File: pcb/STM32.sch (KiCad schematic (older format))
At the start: 31 parts, among them J1 Conn_02x07_Odd_Even, X1 ABM8G

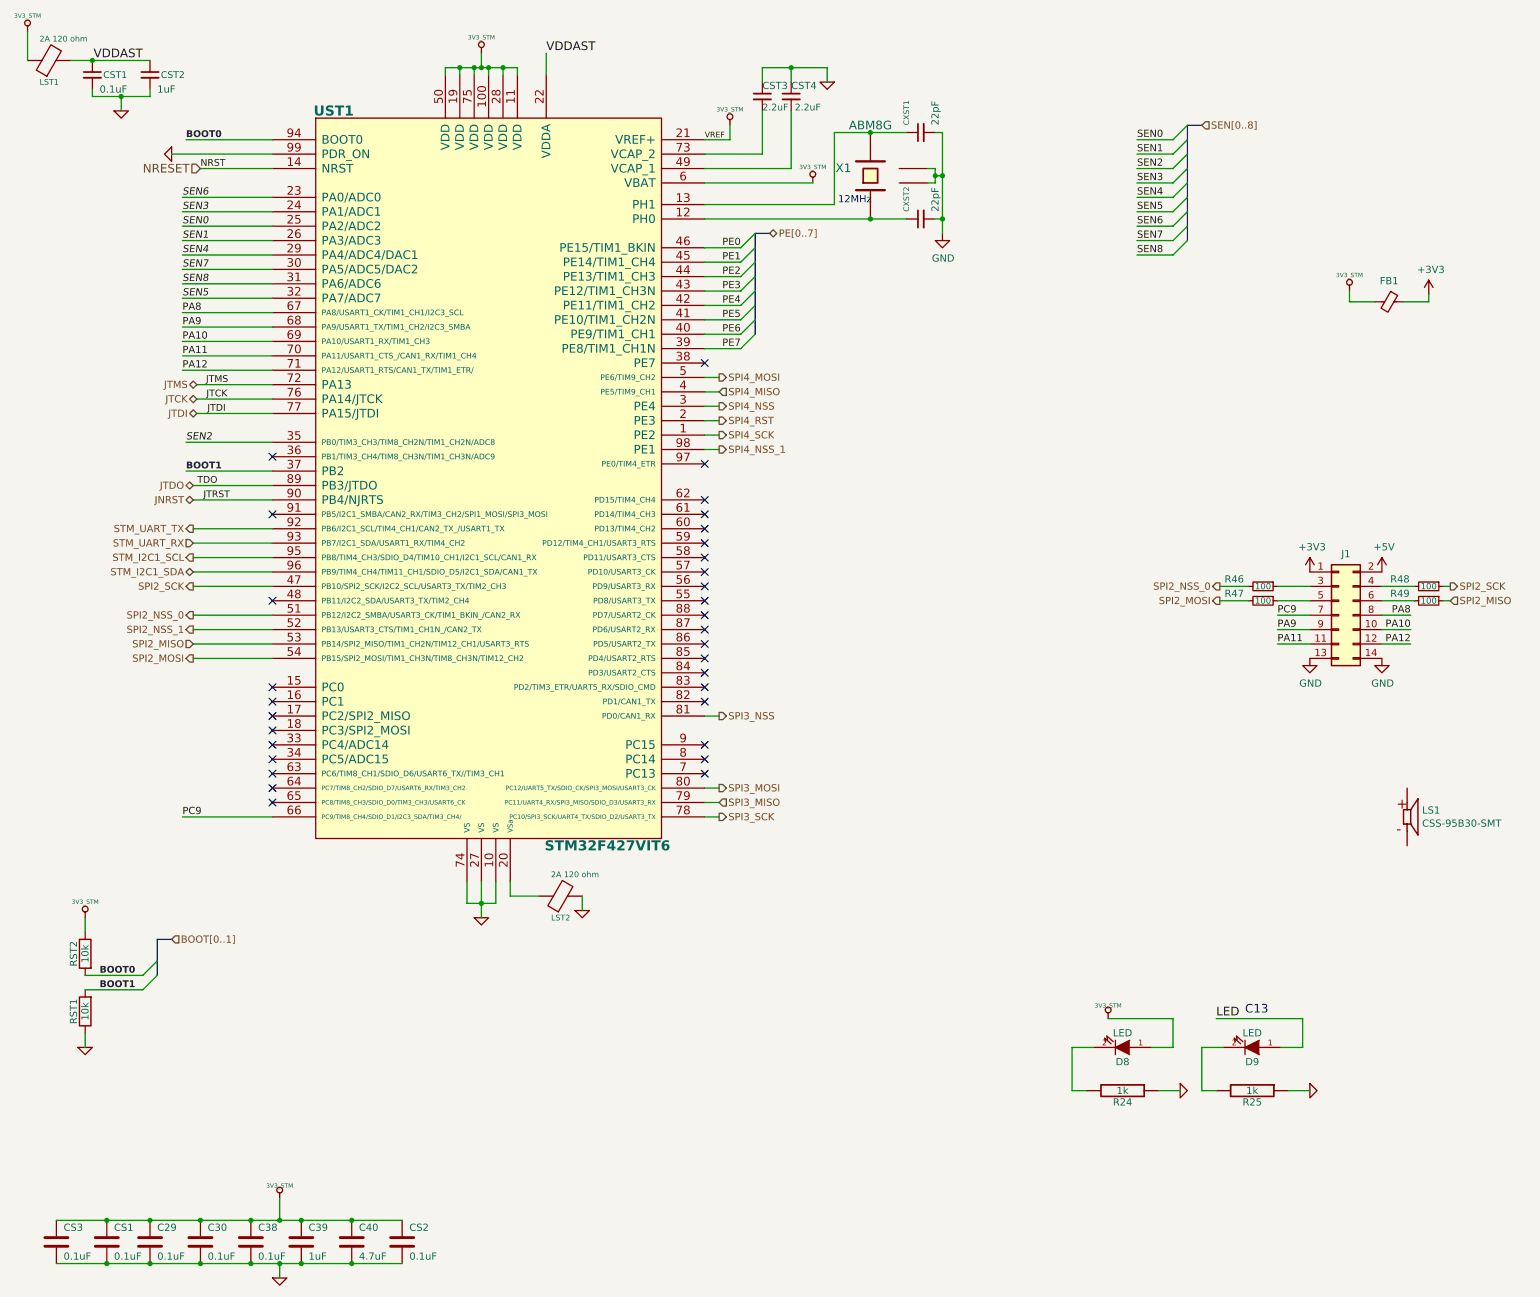
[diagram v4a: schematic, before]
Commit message: Buzzer circuit on schema
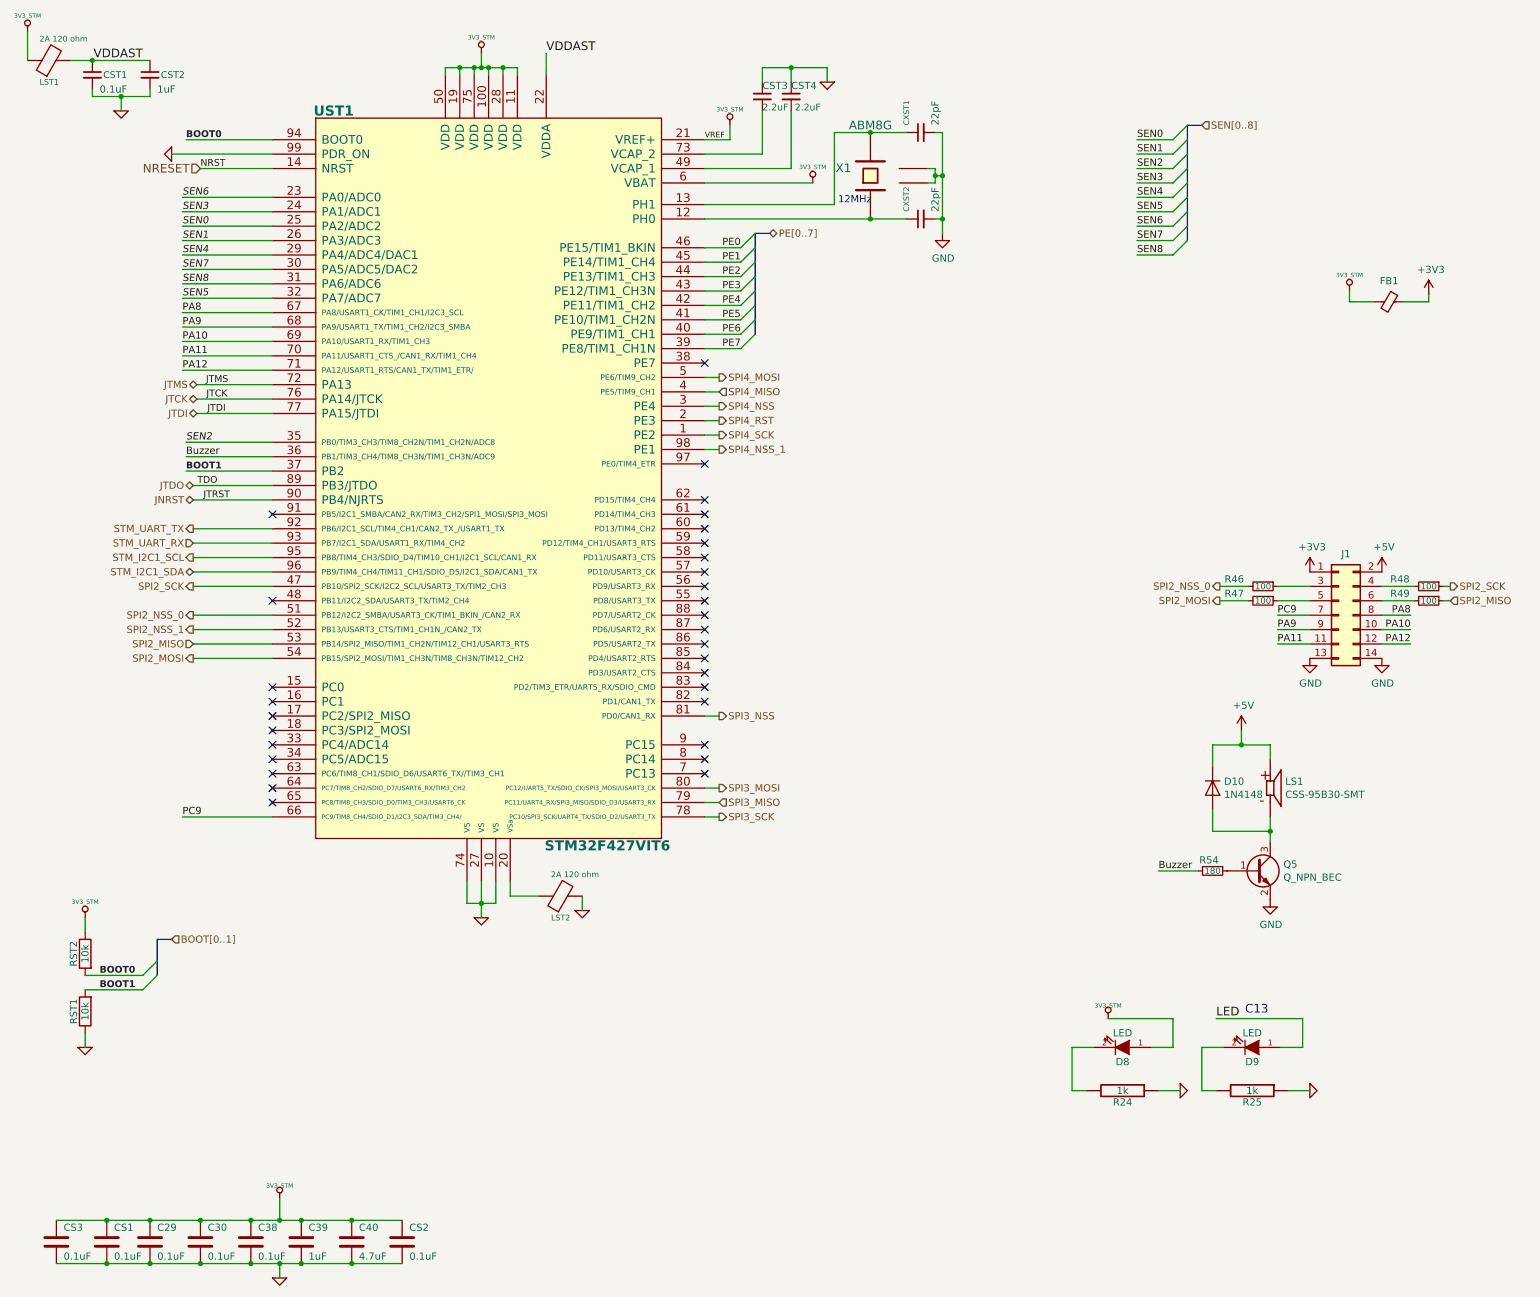
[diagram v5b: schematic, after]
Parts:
- added D10: 1N4148, Diode_THT:D_DO-35_SOD27_P7.62mm_Horizontal, symbol Diode:1N4148
- added Q5: Q_NPN_BEC, SMD:2SC3325-Y, symbol Device:Q_NPN_BEC
- added R54: 180, Resistor_SMD:R_0402_1005Metric, symbol Device:R_Small
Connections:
- net +5V: now also LS1.P, D10.1 (K)
- net GND: now also Q5.2 (E)
- net Buzzer: now reaches UST1.36 (PB1/TIM3_CH4/TIM8_CH3N/TIM1_CH3N/ADC9)
- net Buzzer: now also R54.2
- net at LS1.N: now also D10.2 (A), Q5.3 (C)
- new net: Q5.1 (B), R54.1
- no-connect marks 32 -> 31
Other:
- moved on the sheet: LS1
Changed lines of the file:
@@
 L CSS-95B30-SMT:CSS-95B30-SMT LS1
 U 1 1 5EBB81C9
-P 10475 6100
-F 0 "LS1" H 10579 6146 50  0000 L CNN
-F 1 "CSS-95B30-SMT" H 10579 6055 50  0000 L CNN
-F 2 "SMD:CUI_CSS-95B30-SMT" H 10475 6100 50  0001 L BNN
-F 3 "CSS-95B30-SMT" H 10475 6100 50  0001 L BNN
-F 4 "None" H 10475 6100 50  0001 L BNN "Field4"
-F 5 "CUI" H 10475 6100 50  0001 L BNN "Field5"
-F 6 "None" H 10475 6100 50  0001 L BNN "Field6"
-F 7 "Unavailable" H 10475 6100 50  0001 L BNN "Field7"
-F 8 "10 mm, 5 V, 92 dB, Surface Mount _SMT_, Magnetic Audio Transducer Buzzer" H 10475 6100 50  0001 L BNN "Field8"
-	1    10475 6100
+P 9525 5900
+F 0 "LS1" H 9629 5946 50  0000 L CNN
+F 1 "CSS-95B30-SMT" H 9629 5855 50  0000 L CNN
+F 2 "SMD:CUI_CSS-95B30-SMT" H 9525 5900 50  0001 L BNN
+F 3 "CSS-95B30-SMT" H 9525 5900 50  0001 L BNN
+F 4 "None" H 9525 5900 50  0001 L BNN "Field4"
+F 5 "CUI" H 9525 5900 50  0001 L BNN "Field5"
+F 6 "None" H 9525 5900 50  0001 L BNN "Field6"
+F 7 "Unavailable" H 9525 5900 50  0001 L BNN "Field7"
+F 8 "10 mm, 5 V, 92 dB, Surface Mount _SMT_, Magnetic Audio Transducer Buzzer" H 9525 5900 50  0001 L BNN "Field8"
+	1    9525 5900
 	1    0    0    -1
 $EndComp
@@
 NoConn ~ 2600 5900
 NoConn ~ 2600 6000
-NoConn ~ 2600 3600
 NoConn ~ 2600 4000
+$Comp
+L Diode:1N4148 D10
+U 1 1 5ECD7ACA
+P 9125 5900
+F 0 "D10" V 9079 5979 50  0000 L CNN
+F 1 "1N4148" V 9170 5979 50  0000 L CNN
+F 2 "Diode_THT:D_DO-35_SOD27_P7.62mm_Horizontal" H 9125 5725 50  0001 C CNN
+F 3 "http://www.nxp.com/documents/data_sheet/1N4148_1N4448.pdf" H 9125 5900 50  0001 C CNN
+	1    9125 5900
+	0    1    1    0
+$EndComp
+Wire Wire Line
+	9525 6100 9525 6200
+Wire Wire Line
+	9125 6050 9125 6200
+Wire Wire Line
+	9125 6200 9525 6200
+Connection ~ 9525 6200
+Wire Wire Line
+	9525 6200 9525 6275
+Wire Wire Line
+	9125 5750 9125 5600
+Wire Wire Line
+	9125 5600 9325 5600
+Wire Wire Line
+	9525 5600 9525 5700
+$Comp
+L power:GND #PWR0121
+U 1 1 5ECFAD9D
+P 9525 6675
+F 0 "#PWR0121" H 9525 6425 50  0001 C CNN
+F 1 "GND" H 9530 6502 50  0000 C CNN
+F 2 "" H 9525 6675 50  0001 C CNN
+F 3 "" H 9525 6675 50  0001 C CNN
+	1    9525 6675
+	1    0    0    -1
+$EndComp
+$Comp
+L Device:R_Small R?
+U 1 1 5ECFC0B6
+P 9125 6475
+AR Path="/5E96F696/5ECFC0B6" Ref="R?"  Part="1"
+AR Path="/5E989259/5ECFC0B6" Ref="R54"  Part="1"
+F 0 "R54" V 9050 6450 50  0000 C CNN
+F 1 "180" V 9125 6475 43  0000 C CNN
+F 2 "Resistor_SMD:R_0402_1005Metric" V 9055 6475 50  0001 C CNN
+F 3 "~" H 9125 6475 50  0001 C CNN
+	1    9125 6475
+	0    1    1    0
+$EndComp
+Wire Wire Line
+	8750 6475 9025 6475
+Text Label 8750 6475 0    50   ~ 0
+Buzzer
+$Comp
+L power:+5V #PWR0154
+U 1 1 5ED29E2F
+P 9325 5500
+F 0 "#PWR0154" H 9325 5350 50  0001 C CNN
+F 1 "+5V" H 9340 5673 50  0000 C CNN
+F 2 "" H 9325 5500 50  0001 C CNN
+F 3 "" H 9325 5500 50  0001 C CNN
+	1    9325 5500
+	1    0    0    -1
+$EndComp
+Wire Wire Line
+	9325 5500 9325 5600
+Connection ~ 9325 5600
+Wire Wire Line
+	9325 5600 9525 5600
+Text Label 2000 3600 0    50   ~ 0
+Buzzer
+Wire Wire Line
+	2000 3600 2600 3600
 Wire Bus Line
 	1800 6950 1800 7200
@@
 Wire Bus Line
 	8950 1300 8950 2100
+$Comp
+L Device:Q_NPN_BEC Q5
+U 1 1 5ED67574
+P 9425 6475
+F 0 "Q5" H 9616 6521 50  0000 L CNN
+F 1 "Q_NPN_BEC" H 9616 6430 50  0000 L CNN
+F 2 "SMD:2SC3325-Y" H 9625 6575 50  0001 C CNN
+F 3 "~" H 9425 6475 50  0001 C CNN
+F 4 "2SC3325-YLFTR-ND" H 9425 6475 50  0001 C CNN "DigiKey"
+	1    9425 6475
+	1    0    0    -1
+$EndComp
 $EndSCHEMATC

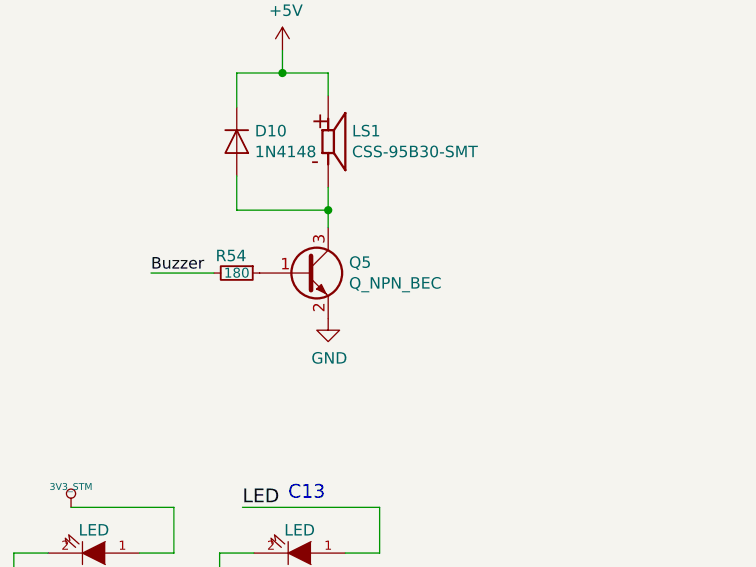
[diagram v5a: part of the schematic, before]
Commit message: Buzzer circuit on PCB
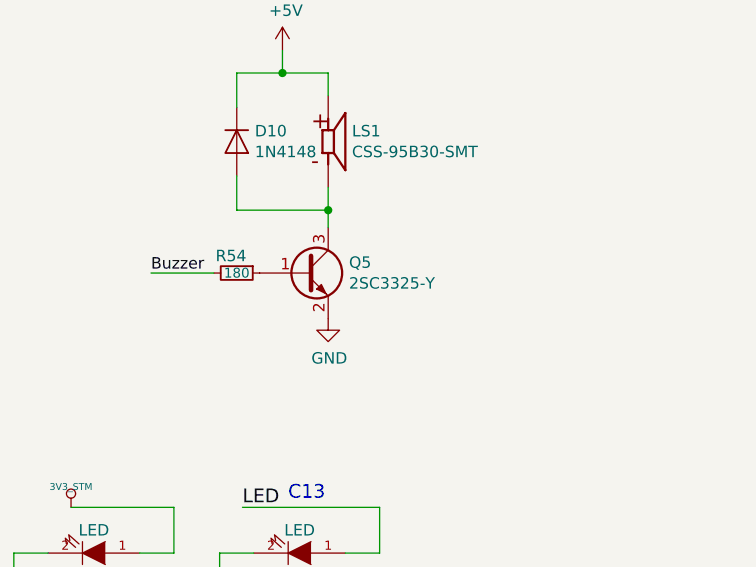
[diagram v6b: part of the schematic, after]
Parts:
- Q5: value Q_NPN_BEC -> 2SC3325-Y
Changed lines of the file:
@@
 Wire Wire Line
 	2000 3600 2600 3600
+$Comp
+L Device:Q_NPN_BEC Q5
+U 1 1 5ED67574
+P 9425 6475
+F 0 "Q5" H 9616 6521 50  0000 L CNN
+F 1 "2SC3325-Y" H 9616 6430 50  0000 L CNN
+F 2 "SMD:2SC3325-Y" H 9625 6575 50  0001 C CNN
+F 3 "~" H 9425 6475 50  0001 C CNN
+F 4 "2SC3325-YLFTR-ND" H 9425 6475 50  0001 C CNN "DigiKey"
+	1    9425 6475
+	1    0    0    -1
+$EndComp
 Wire Bus Line
 	1800 6950 1800 7200
@@
 Wire Bus Line
 	8950 1300 8950 2100
-$Comp
-L Device:Q_NPN_BEC Q5
-U 1 1 5ED67574
-P 9425 6475
-F 0 "Q5" H 9616 6521 50  0000 L CNN
-F 1 "Q_NPN_BEC" H 9616 6430 50  0000 L CNN
-F 2 "SMD:2SC3325-Y" H 9625 6575 50  0001 C CNN
-F 3 "~" H 9425 6475 50  0001 C CNN
-F 4 "2SC3325-YLFTR-ND" H 9425 6475 50  0001 C CNN "DigiKey"
-	1    9425 6475
-	1    0    0    -1
-$EndComp
 $EndSCHEMATC

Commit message: Solved problems with POWERSTEP01 footprint
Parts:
- D10: footprint Diode_THT:D_DO-35_SOD27_P7.62mm_Horizontal -> Diode_SMD:D_SOD-123; DigiKey (none) -> 1655-1360-1-ND
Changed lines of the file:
@@
 F 0 "D10" V 9079 5979 50  0000 L CNN
 F 1 "1N4148" V 9170 5979 50  0000 L CNN
-F 2 "Diode_THT:D_DO-35_SOD27_P7.62mm_Horizontal" H 9125 5725 50  0001 C CNN
+F 2 "Diode_SMD:D_SOD-123" H 9125 5725 50  0001 C CNN
 F 3 "http://www.nxp.com/documents/data_sheet/1N4148_1N4448.pdf" H 9125 5900 50  0001 C CNN
+F 4 "1655-1360-1-ND" V 9125 5900 50  0001 C CNN "DigiKey"
 	1    9125 5900
 	0    1    1    0
